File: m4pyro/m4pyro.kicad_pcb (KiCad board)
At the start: 2 copper layers, 100 x 75 mm, 162 parts, among them IC1 STM32F405RxTx, IC10 LTC4151, IC2 TPS62133, IC3 MCP2562, IC4 TPS62153, IC5 ADP2389, IC6 LTC4151, IC7 ADP2389, IC8 LTC4151, IC9 ADP2389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

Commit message: continued pyro board layout
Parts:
- moved R10 260.3 mm to (16.1, 93.3)
- moved R4 255.6 mm to (32.4, 96.9)
- moved R2 250.5 mm to (31.6, 101.6)
- moved R9 247.3 mm to (15.8, 90.2)
- moved D1 245.1 mm to (32.5, 105.3)
- moved R5 227.2 mm to (21.6, 92.6)
- moved C8 223.3 mm to (26.6, 88.0)
- moved P1 217.2 mm to (27.1, 83.6)
- moved R7 212.8 mm to (20.8, 91.3)
- moved D2 211.6 mm to (22.4, 99.6)
- moved R3 211.6 mm to (28.4, 99.1)
- moved D3 200.8 mm to (35.1, 92.9)
- moved R41 177.4 mm to (82.4, 107.3)
- moved C22 175.6 mm to (111.7, 100.6), turned to 90 degrees
- moved C25 170.9 mm to (104.9, 87.8), turned to 90 degrees
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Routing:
- net /BUS: track 0.00 -> 122.5 mm, vias 0 -> 10
- net /PYRO4: track 3.28 -> 60.4 mm, vias 1 -> 2
- net /CH8_CONT: track 0.00 -> 56.2 mm
- net /PYRO6: track 3.30 -> 53.0 mm, vias 1 -> 2
- net /PYRO_SI: track 198.3 -> 245.2 mm
- net /PYRO5: track 3.30 -> 49.6 mm
- net /PYRO2: track 3.22 -> 46.7 mm, vias 1 -> 2
- net /PYRO3: track 3.28 -> 44.5 mm
- net /CH8: track 0.00 -> 38.7 mm
- net /PYRO7: track 3.24 -> 40.0 mm
- net /CH7_CONT: track 0.00 -> 32.2 mm
- net /CH7: track 0.00 -> 30.7 mm
- net /PYRO8: track 3.24 -> 30.3 mm, vias 1 -> 2
- net /CH6_CONT: track 0.00 -> 24.5 mm
- net /PYRO1: track 3.22 -> 26.1 mm
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
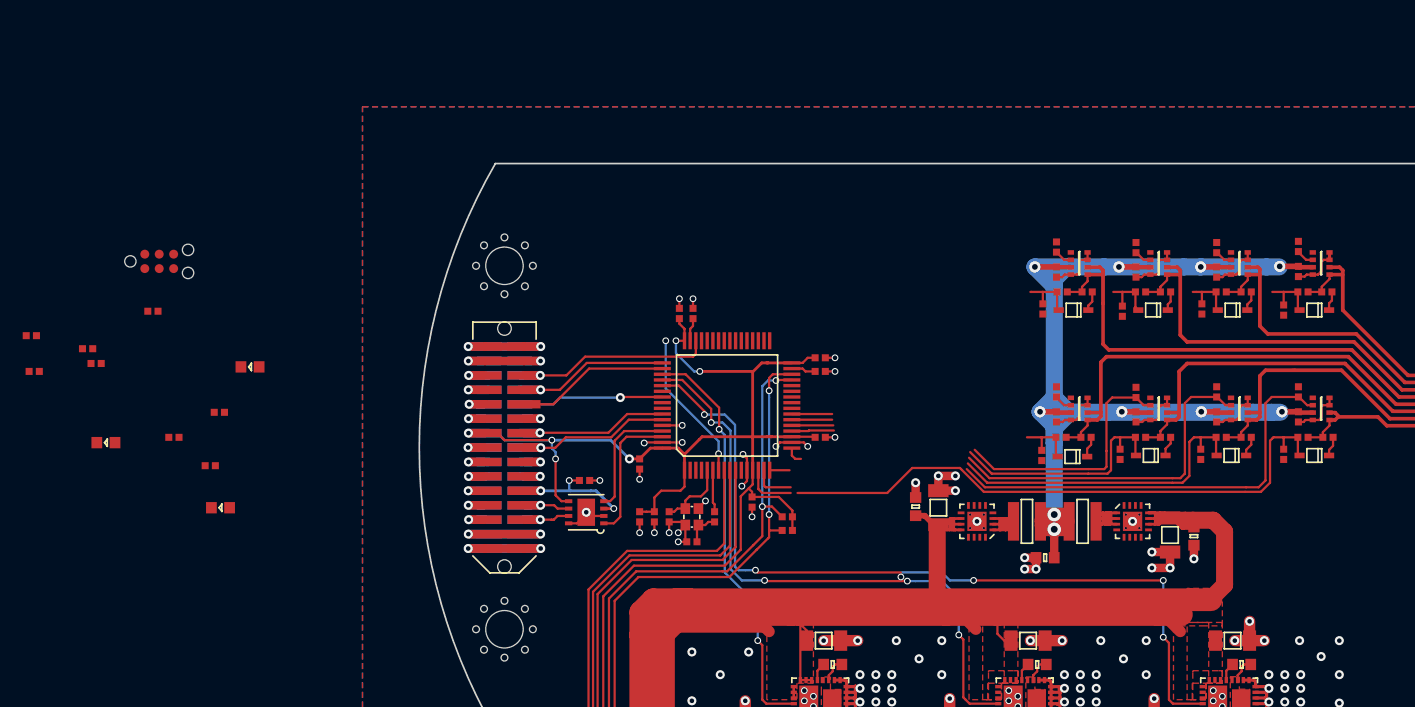
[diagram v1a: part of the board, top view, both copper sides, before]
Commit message: made good progress on pyro routing
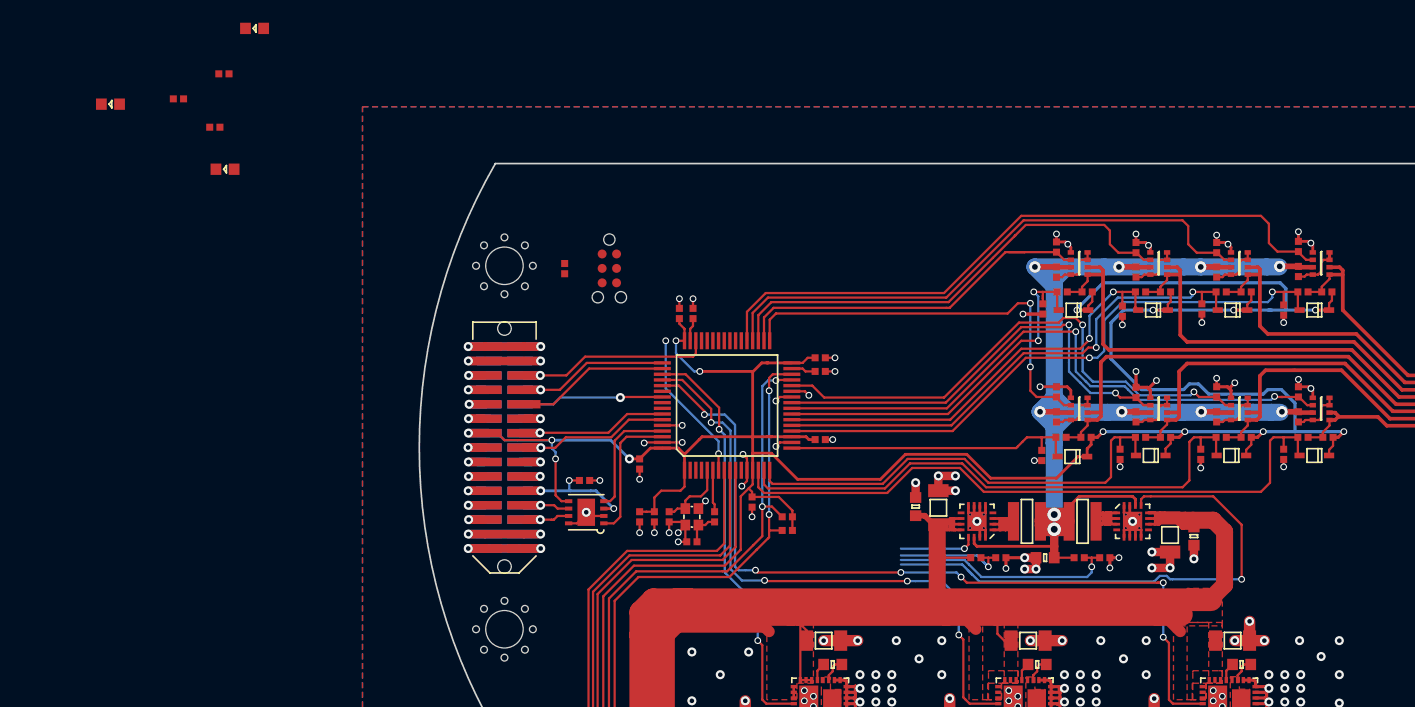
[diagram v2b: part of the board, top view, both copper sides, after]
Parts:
- moved R10 95.7 mm to (110.3, 109.7)
- moved R9 94.3 mm to (108.1, 109.7)
- moved R5 81.5 mm to (101.2, 109.7)
- moved R7 80.3 mm to (99.0, 109.7)
- moved P1 39.6 mm to (66.7, 84.2), turned to 270 degrees
- moved C8 36.4 mm to (62.8, 84.2), turned to 90 degrees
- moved R4 29.8 mm to (32.8, 67.1)
- moved D3 29.8 mm to (35.5, 63.1)
- moved D1 29.8 mm to (32.9, 75.5)
- moved D2 29.8 mm to (22.8, 69.8)
- moved R2 29.8 mm to (32.0, 71.8)
- moved R3 29.8 mm to (28.8, 69.3)
- moved C10 0.20 mm to (85.3, 99.3)
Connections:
- IC1 pad 14: /CH1_CONT -> /CH8_CONT
- IC1 pad 15: /CH2_CONT -> /CH7_CONT
- IC1 pad 16: /CH3_CONT -> /CH6_CONT
- IC1 pad 17: /CH4_CONT -> /CH5_CONT
- IC1 pad 2: /LED_RED -> (no net)
- IC1 pad 20: /CH5_CONT -> /CH1_CONT
- IC1 pad 21: /CH6_CONT -> /CH2_CONT
- IC1 pad 22: /CH7_CONT -> /CH3_CONT
- IC1 pad 23: /CH8_CONT -> /CH4_CONT
- IC1 pad 24: /CH4 -> /CH8
- IC1 pad 25: /CH8 -> /CH6
- IC1 pad 28: (no net) -> /CH7
- IC1 pad 3: /LED_YLW -> (no net)
- IC1 pad 33: /CH1 -> /CH5
- IC1 pad 34: /CH5 -> /CH4
- IC1 pad 35: (no net) -> /CH3
- IC1 pad 37: /CH6 -> /CH1
- IC1 pad 38: /CH3 -> (no net)
- IC1 pad 39: /CH7 -> (no net)
- IC1 pad 4: /LED_GRN -> (no net)
- IC1 pad 40: (no net) -> /LED_GRN
- IC1 pad 41: (no net) -> /LED_YLW
- IC1 pad 42: (no net) -> /LED_RED
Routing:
- net 3v3: track 175.3 -> 303.9 mm, vias 6 -> 14
- net /CH1: track 1.69 -> 58.6 mm
- net GND: track 250.2 -> 306.7 mm, vias 167 -> 192
- net /CH2: track 1.52 -> 50.3 mm
- net /1A_EN: track 0.00 -> 46.9 mm, vias 0 -> 1
- net /CH1_CONT: track 9.71 -> 54.3 mm, vias 0 -> 2
- net /CH3: track 1.52 -> 42.2 mm
- net /CH2_CONT: track 8.52 -> 46.6 mm, vias 0 -> 2
- net /CH5: track 1.59 -> 37.2 mm, vias 0 -> 2
- net /CH3_CONT: track 6.65 -> 39.1 mm, vias 0 -> 2
- net /CH4: track 1.54 -> 33.1 mm
- net /CH4_CONT: track 6.64 -> 33.9 mm, vias 0 -> 2
- net /BUS_DIV: track 0.00 -> 21.9 mm, vias 0 -> 2
- net /BUS: track 122.5 -> 140.1 mm
- net /CH6: track 22.3 -> 39.7 mm, vias 0 -> 2
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
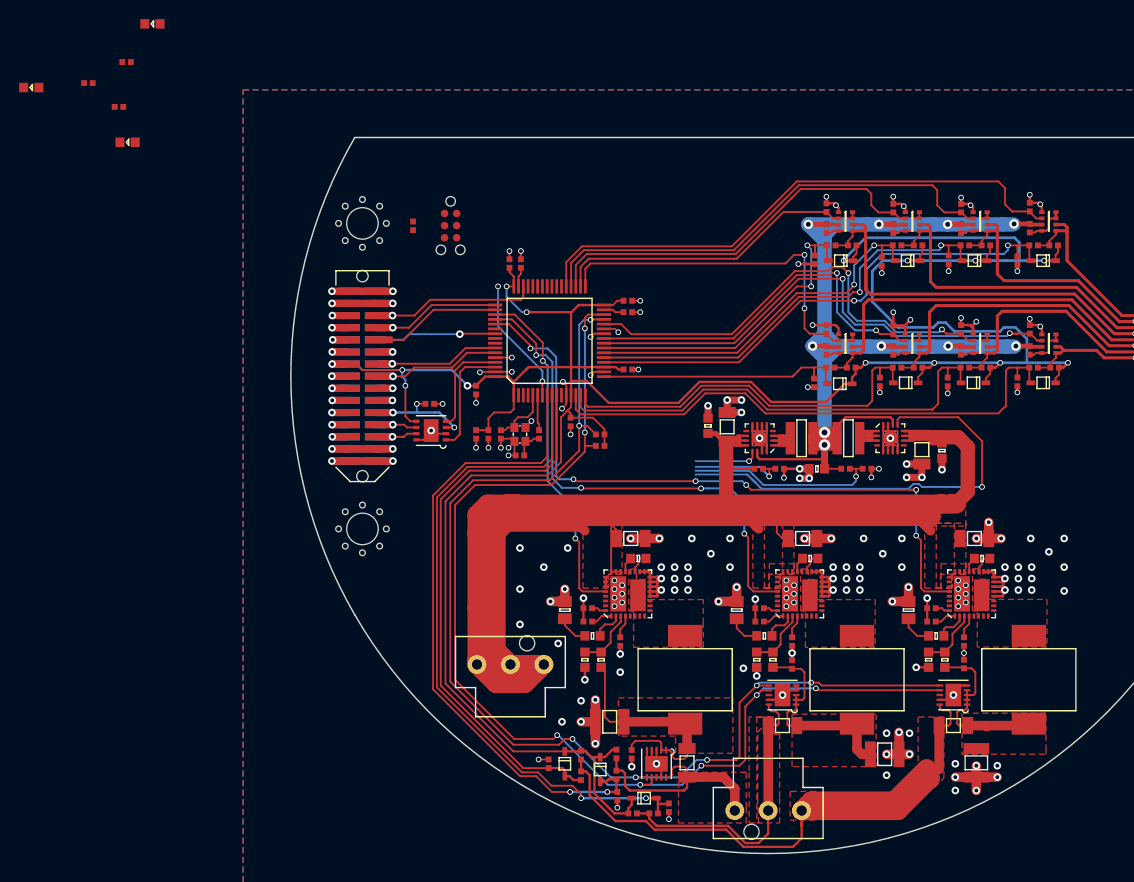
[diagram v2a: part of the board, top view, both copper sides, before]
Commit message: routed pyro board
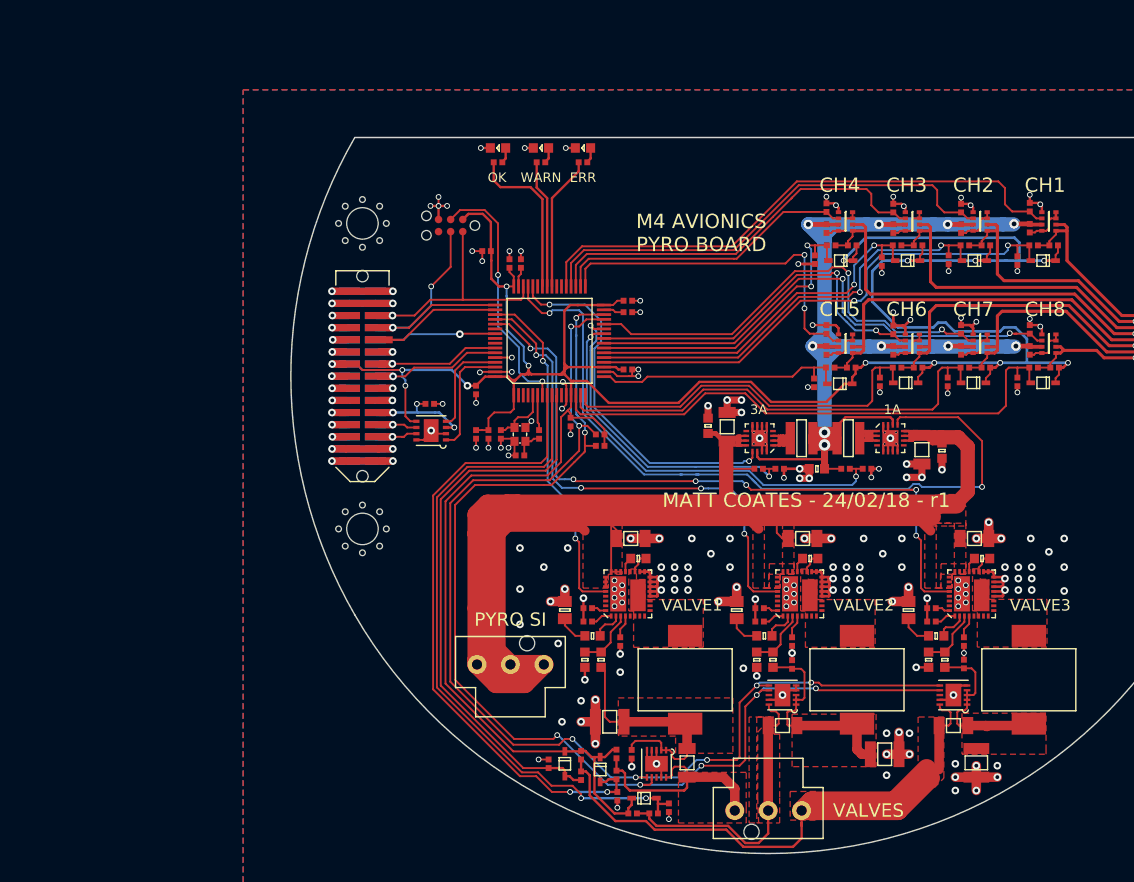
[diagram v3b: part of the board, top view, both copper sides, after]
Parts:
- moved D2 53.8 mm to (76.2, 76.1)
- moved R2 48.9 mm to (80.6, 77.6)
- moved R3 48.1 mm to (76.2, 77.6)
- moved D1 47.7 mm to (80.6, 76.1)
- moved R4 40.3 mm to (71.7, 77.6)
- moved D3 38.5 mm to (71.7, 76.1)
- moved C8 8.14 mm to (70.5, 86.9), turned to 0 degrees
- turned P1 to 180 degrees
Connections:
- IC1 pad 26: /SI_DIV -> /BUS_DIV
- IC1 pad 27: /BUS_DIV -> /SI_DIV
- IC1 pad 40: /LED_GRN -> /LED_RED
- IC1 pad 42: /LED_RED -> /LED_GRN
- IC1 pad 44: /1A_EN -> /3A_EN
- IC1 pad 45: /3A_EN -> /1A_EN
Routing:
- net /1A_EN: track 46.9 -> 80.2 mm, vias 1 -> 2
- net /3A_EN: track 6.74 -> 38.5 mm, vias 1 -> 2
- net /SI_DIV: track 12.7 -> 35.5 mm
- net /BUS_DIV: track 21.9 -> 43.7 mm
- net 3v3: track 303.9 -> 321.7 mm
- net /LED_GRN: track 0.00 -> 17.0 mm
- net /LED_RED: track 0.00 -> 14.2 mm
- net /JTCK: track 15.0 -> 28.5 mm, vias 1 -> 2
- net /LED_YLW: track 0.00 -> 13.5 mm
- net /~RST: track 13.3 -> 26.8 mm
- net GND: track 306.7 -> 318.8 mm, vias 192 -> 201
- net /JTMS: track 18.9 -> 26.0 mm
- net Net-(D1-Pad2): track 0.00 -> 1.64 mm
- net Net-(D3-Pad2): track 0.00 -> 1.64 mm
- net Net-(D2-Pad2): track 0.00 -> 1.64 mm
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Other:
- board text added: "1A"
- board text added: "3A"
- board text added: "CH1"
- board text added: "CH2"
- board text added: "CH3"
- board text added: "CH4"
- board text added: "CH5"
- board text added: "CH6"
- board text added: "CH7"
- board text added: "CH8"
- board text added: "ERR"
- board text added: "M4 AVIONICS PYRO BOARD"
- board text added: "MATT COATES - 24/02/18 - r1"
- board text added: "OK"
- board text added: "PYRO SI"
- board text added: "VALVE1"
- board text added: "VALVE2"
- board text added: "VALVE3"
- board text added: "VALVES"
- board text added: "WARN"

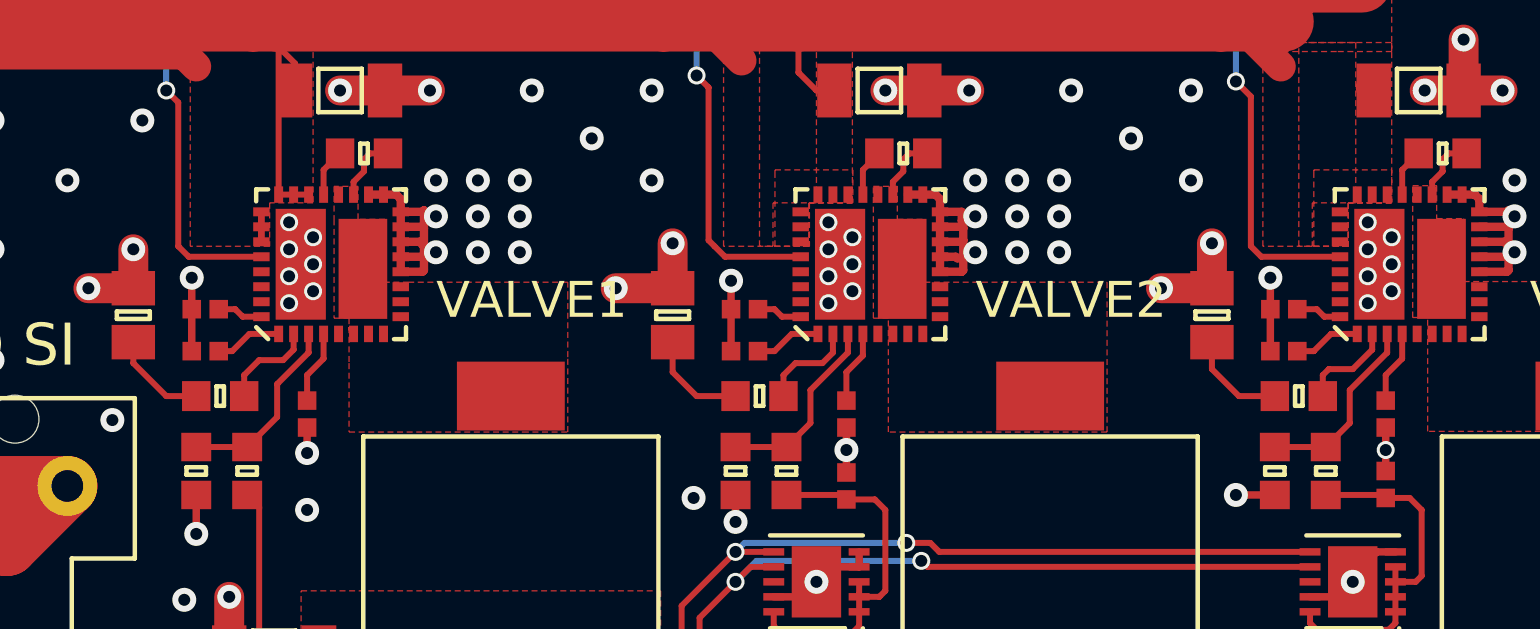
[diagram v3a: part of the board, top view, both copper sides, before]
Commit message: added ilim resistor to pyro board
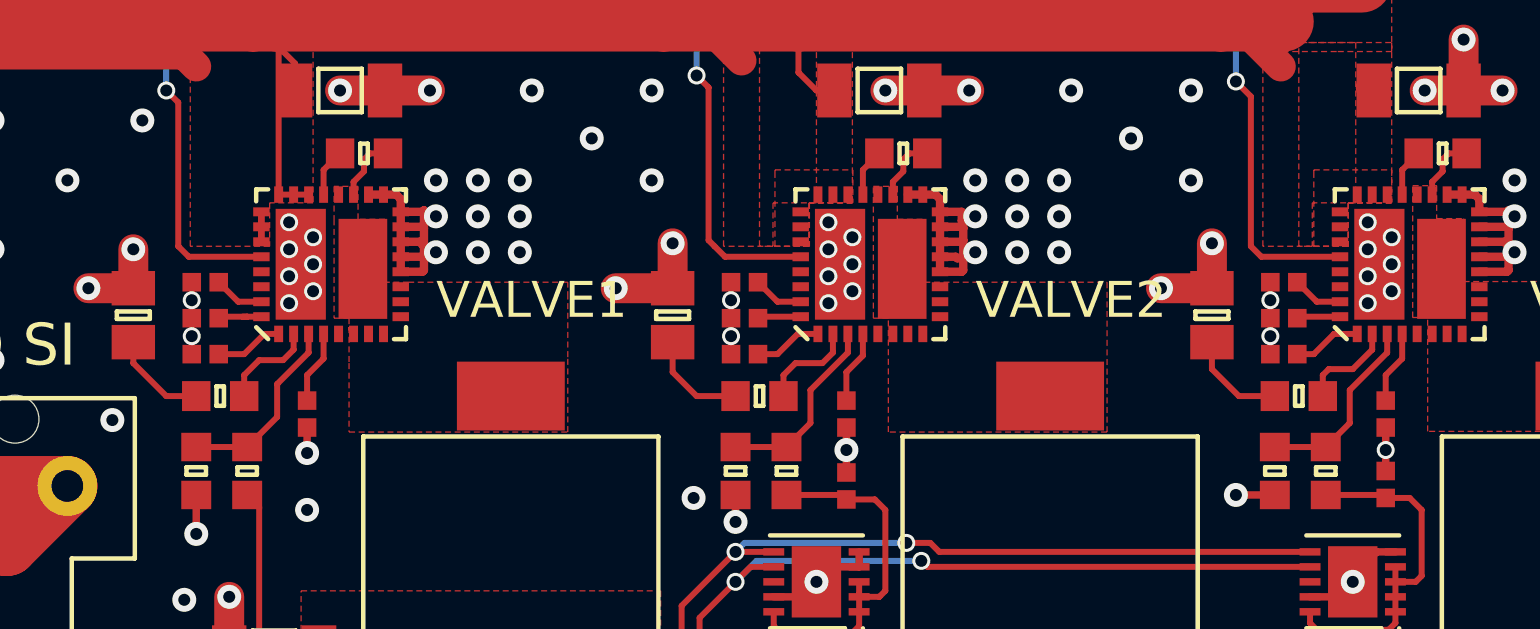
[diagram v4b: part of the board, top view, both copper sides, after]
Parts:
- added R64: 82.5k, agg:0402, F.Cu at (81.1, 123.4)
- added R65: 82.5k, agg:0402, F.Cu at (99.1, 123.4)
- added R66: 82.5k, agg:0402, F.Cu at (117.1, 123.4)
- moved R43 0.30 mm to (81.1, 124.6)
- moved R48 0.30 mm to (99.1, 124.6)
- moved R53 0.30 mm to (117.1, 124.6)
- moved C31 0.10 mm to (81.1, 125.8)
- moved C38 0.10 mm to (99.1, 125.8)
- moved C45 0.10 mm to (117.1, 125.8)
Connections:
- IC5 pad 31: (no net) -> Net-(IC5-Pad31)
- IC7 pad 31: (no net) -> Net-(IC7-Pad31)
- IC9 pad 31: (no net) -> Net-(IC9-Pad31)
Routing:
- net Net-(IC9-Pad31): track 0.00 -> 1.69 mm
- net Net-(IC7-Pad31): track 0.00 -> 1.69 mm
- net Net-(IC5-Pad31): track 0.00 -> 1.69 mm
- net GND: track 318.8 -> 318.7 mm, vias 201 -> 204
